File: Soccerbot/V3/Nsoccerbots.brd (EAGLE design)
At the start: 149.8 x 101.3 mm, 69 parts, among them CN2 1X4-CLEANBIG, IC1 LM340S-05, IC2 TB6612FNG, IC4 TB6612FNG, J3 1X5, J4 1X5, Q1 AOD417, SW2 SPST_TACT-EVQQ2, U1 PCA9685, X1 NXT-SOCKET, X2 NXT-SOCKET, X3 NXT-SOCKET, X4 NXT-SOCKET

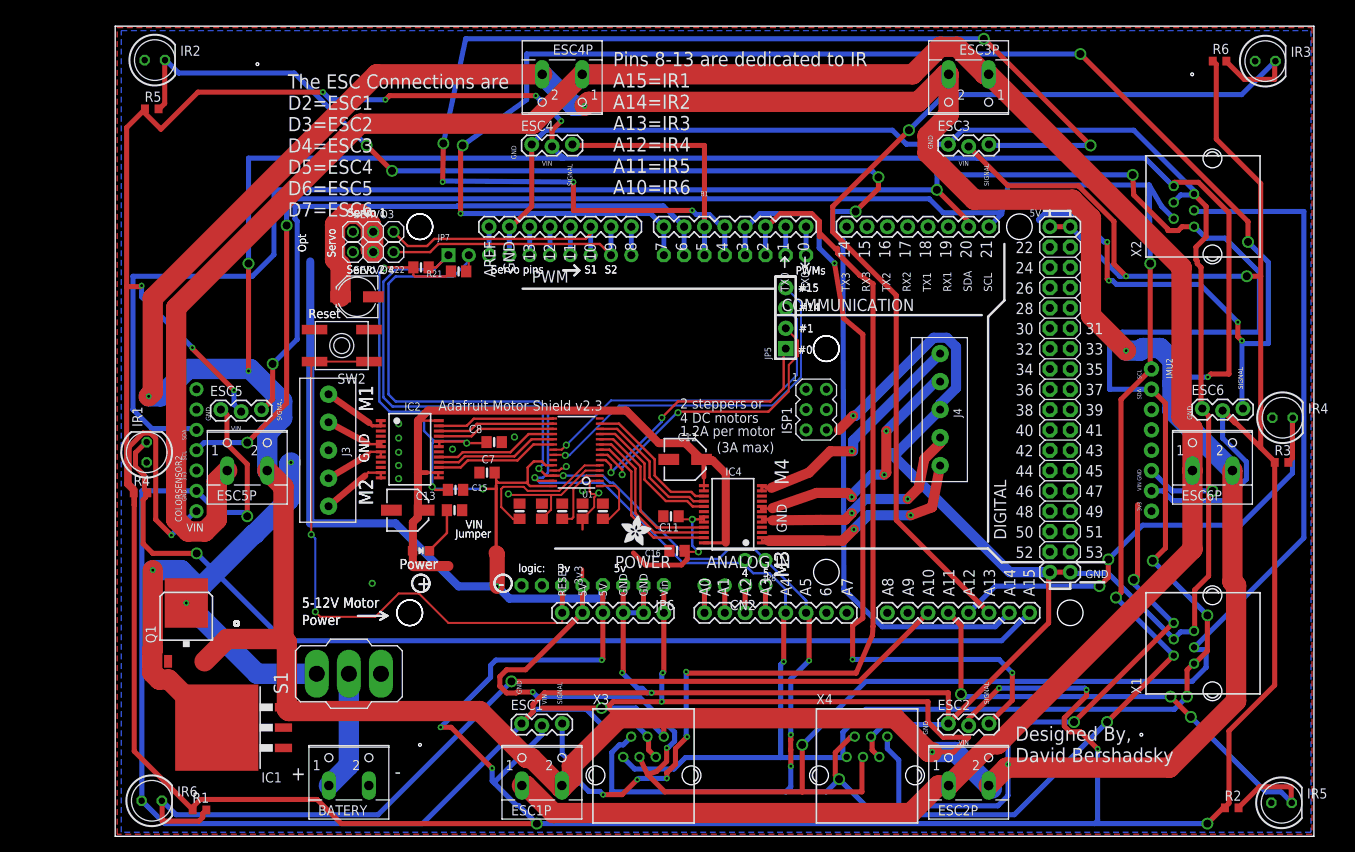
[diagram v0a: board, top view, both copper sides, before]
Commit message: Fully routed and all parts in
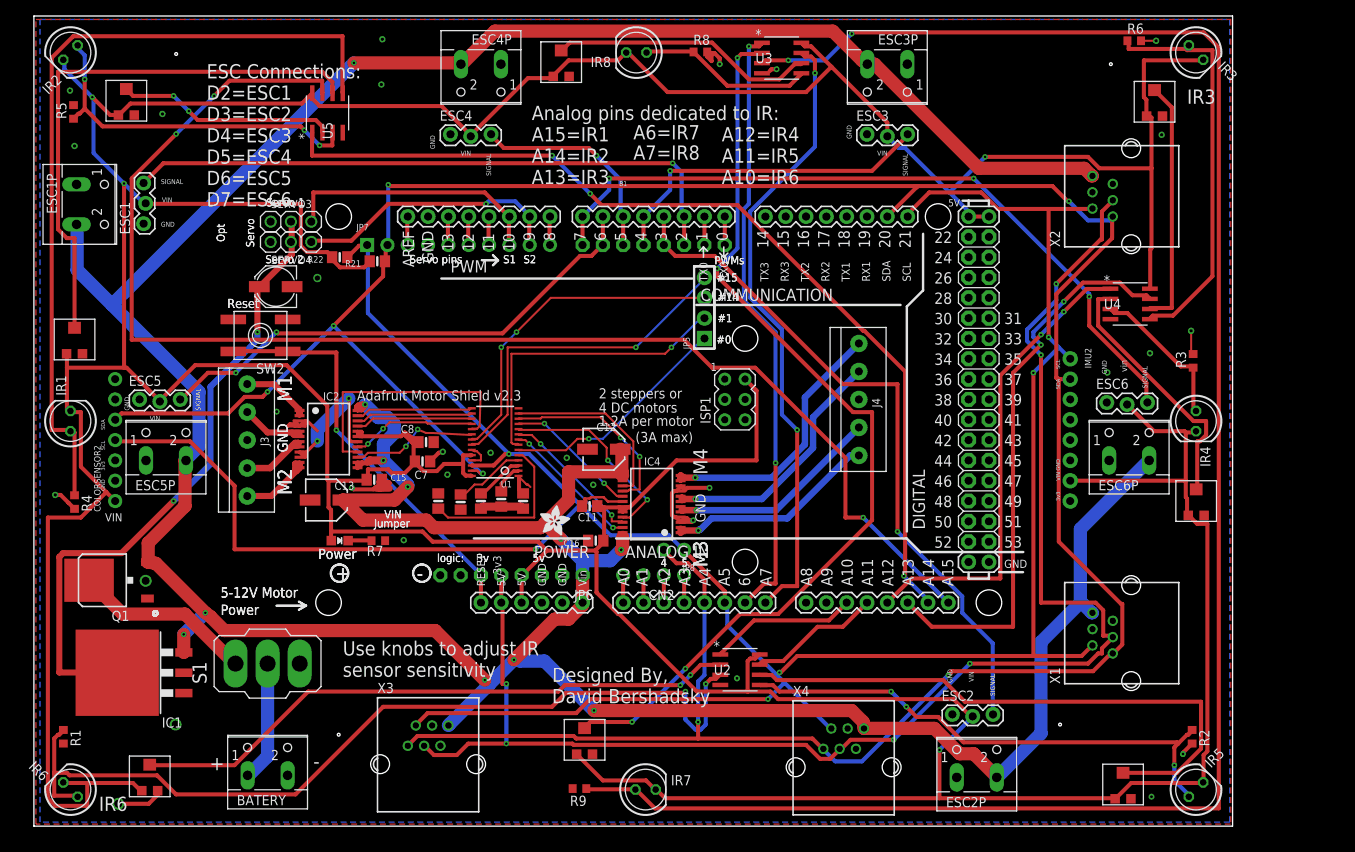
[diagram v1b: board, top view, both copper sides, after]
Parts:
- removed R18: 1K, microbuilder:0805-NO
- added IR7, IR8: (no value), led:LED5MM
- added IRP1, IRP2, IRP3, IRP4, IRP5, IRP6, IRP7, IRP8: TRIMPOT, trimPot:TRIMPOT
- added R7: 300ohm, rcl:R0603
- added R8, R9: 10k, adafruit:R0603
- added U2, U3, U4, U5: LM358DT, LM358DT:D8
- R1, R2, R3, R4, R5, R6: value (none) -> 10k
- moved ESC1P 91.3 mm to (6.60, 77.7), turned to 270 degrees
- moved ESC1 78.4 mm to (13.8, 75.3), turned to 90 degrees
- moved X3 27.0 mm to (49.3, 7.75)
- moved R1 19.3 mm to (3.68, 11.2), turned to 270 degrees
- moved R3 16.8 mm to (144.9, 58.2), turned to 90 degrees
- moved IC1 14.2 mm to (13.0, 19.2)
- moved ESC6 12.0 mm to (134.1, 52.8)
- moved Q1 11.0 mm to (9.40, 30.7), turned to 90 degrees
- moved R6 11.0 mm to (137.5, 98.2)
- moved IR4 10.8 mm to (145.3, 50.6), turned to 270 degrees
- moved IR5 10.8 mm to (145.3, 4.57), turned to 45 degrees
- moved IR2 10.6 mm to (4.57, 96.7), turned to 225 degrees
- moved ESC6P 10.5 mm to (136.9, 47.0)
- moved SERVO3 10.4 mm to (32.1, 75.6)
- moved SERVO4 10.4 mm to (32.1, 73.0)
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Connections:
- removed net GND1: IR5.A
- removed net GND2: IR4.A
- removed net GND3: IR1.A
- removed net GND4: IR2.A
- removed net GND5: IR3.A
- removed net VCC: ISP1.2
- new net IR1O+: IR1.A, R4.1, U5.5
- new net IR2O+: IR2.A, R5.1, U5.3
- new net IR3O+: IR3.A, R6.1, U4.5
- new net IR4O+: IR4.A, R3.1, U4.3
- new net IR5O+: IR5.A, R2.1, U2.5
- new net IR6O+: IR6.A, R1.1, U2.3
- new net IR7O+: IR7.A, R9.1, U3.3
- new net IR8O+: IR8.A, R8.1, U3.5
- new net N$11: IRP6.OUT, U2.2
- new net N$14: IRP5.OUT, U2.6
- new net N$17: IRP8.OUT, U3.6
- new net N$18: IRP3.OUT, U4.6
- new net N$21: IRP4.OUT, U4.2
- new net N$24: IRP2.OUT, U5.2
- new net N$27: IRP1.OUT, U5.6
- new net N$6: IRP7.OUT, U3.2
- net 5.5V: now also IR1.K, IR2.K, IR3.K, IR4.K, IR5.K, IR6.K, IR7.K, IR8.K, IRP1.VCC, IRP2.VCC, IRP3.VCC, IRP4.VCC, IRP5.VCC, IRP6.VCC, IRP7.VCC, IRP8.VCC, ISP1.2, LED2.A, U2.8, U3.8, U4.8, U5.8; no longer R1.1, R2.1, R3.1, R4.1, R5.1, R6.1
- net A10: now also U2.1; no longer IR6.K, R1.2
- net A11: now also U2.7; no longer IR5.K, R2.2
- net A12: now also U4.1; no longer IR4.K, R3.2
- net A13: now also U4.7; no longer IR3.K, R6.2
- net A14: now also U5.1; no longer IR2.K, R5.2
- net A15: now also U5.7; no longer IR1.K, R4.2
- net A6: now also U3.1
- net A7: now also U3.7
- net BAT+: no longer LED2.A
- net GND: now also IRP1.GND, IRP2.GND, IRP3.GND, IRP4.GND, IRP5.GND, IRP6.GND, IRP7.GND, IRP8.GND, R1.2, R2.2, R3.2, R4.2, R5.2, R6.2, R7.1, R8.2, R9.2, U2.4, U3.4, U4.4, U5.4; no longer IR6.A, R18.1
- net N$1: now also R7.2; no longer R18.2
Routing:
- net GND: track 846.5 -> 87.7 mm, vias 15 -> 32
- net BAT+: track 878.3 -> 486.8 mm, vias 13 -> 11
- net IR7O+: track 0.00 -> 234.7 mm, vias 0 -> 2
- net D7: track 217.2 -> 92.3 mm, vias 8 -> 3
- net N$6: track 0.00 -> 118.3 mm, vias 0 -> 4
- net D4: track 157.9 -> 42.3 mm, vias 6 -> 1
- net IR6O+: track 0.00 -> 111.3 mm, vias 0 -> 2
- net SDA: track 473.0 -> 364.5 mm
- net IR1O+: track 0.00 -> 102.0 mm
- net SCL: track 442.7 -> 344.0 mm, vias 11 -> 6
- net A10: track 115.9 -> 18.5 mm, vias 1 -> 0
- net A7: track 0.00 -> 78.4 mm, vias 0 -> 2
- net N$11: track 0.00 -> 76.5 mm, vias 0 -> 2
- net A6: track 0.00 -> 75.7 mm, vias 0 -> 2
- net N$14: track 0.00 -> 73.4 mm
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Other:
- board text added: "A12=IR4 A11=IR5 A10=IR6"
- board text added: "A6=IR7"
- board text added: "A7=IR8"
- board text added: "Analog pins dedicated to IR: A15=IR1 A14=IR2 A13=IR3"
- board text added: "ESC Connections: D2=ESC1 D3=ESC2 D4=ESC3 D5=ESC4 D6=ESC5 D7=ESC6"
- board text added: "IR3"
- board text added: "IR6"
- board text added: "Use knobs to adjust IR sensor sensitivity"
- board text added: "vin"
- board text removed: "Pins 8-13 are dedicated to IR A15=IR1 A14=IR2 A13=IR3 A12=IR4 A11=IR5 A10=IR6"
- board text removed: "The ESC Connections are D2=ESC1 D3=ESC2 D4=ESC3 D5=ESC4 D6=ESC5 D7=ESC6"

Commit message: added resistors
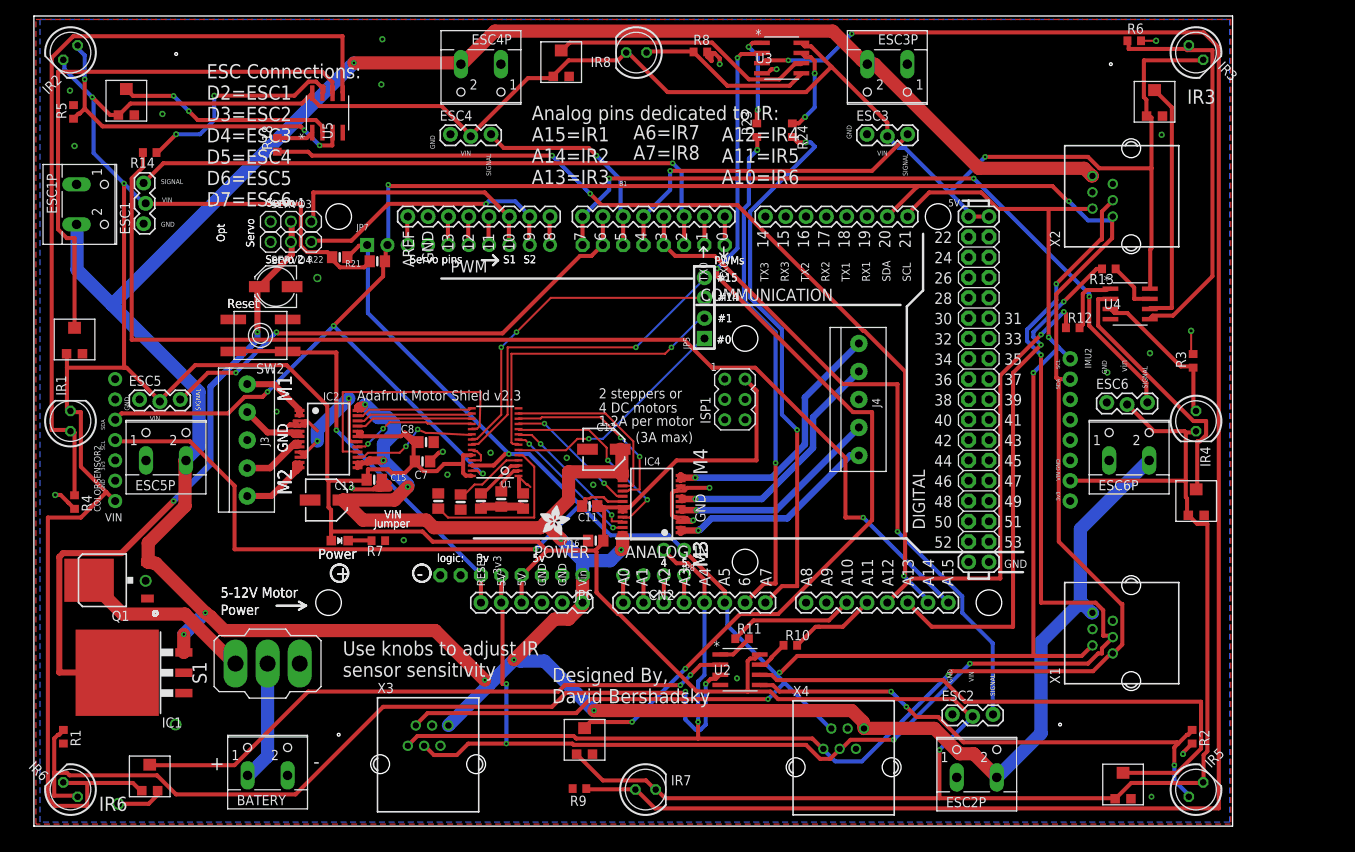
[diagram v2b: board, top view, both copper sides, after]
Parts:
- added R10, R11, R12, R13, R14, R18, R23, R24: 330ohms, resistor:R0603
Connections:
- new net N$10: R14.1, U5.7
- new net N$12: R18.2, U5.1
- new net N$13: R23.2, U3.1
- new net N$15: R24.1, U3.7
- new net N$2: R10.1, U2.7
- new net N$7: R11.2, U2.1
- new net N$8: R12.2, U4.1
- new net N$9: R13.1, U4.7
- net A10: now also R11.1; no longer U2.1
- net A11: now also R10.2; no longer U2.7
- net A12: now also R12.1; no longer U4.1
- net A13: now also R13.2; no longer U4.7
- net A14: now also R18.1; no longer U5.1
- net A15: now also R14.2; no longer U5.7
- net A6: now also R23.1; no longer U3.1
- net A7: now also R24.2; no longer U3.7
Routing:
- net N$10: track 0.00 -> 27.5 mm, vias 0 -> 2
- net A15: track 170.7 -> 144.0 mm, vias 3 -> 1
- net A6: track 75.7 -> 63.0 mm
- net N$13: track 0.00 -> 12.0 mm, vias 0 -> 2
- net N$15: track 0.00 -> 11.5 mm, vias 0 -> 2
- net A7: track 78.4 -> 68.9 mm
- net N$8: track 0.00 -> 8.09 mm
- net N$9: track 0.00 -> 6.67 mm
- net A13: track 71.1 -> 65.0 mm
- net A11: track 16.6 -> 11.2 mm
- net A12: track 59.0 -> 54.1 mm
- net N$12: track 0.00 -> 4.67 mm
- net N$7: track 0.00 -> 4.38 mm
- net N$2: track 0.00 -> 4.03 mm
- net A10: track 18.5 -> 15.8 mm
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
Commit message: x
x
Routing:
- net 5.5V: track 773.9 -> 777.9 mm
- net M1B1: track 8.64 -> 9.96 mm
- net BAT+: track 486.8 -> 488.1 mm
- net GND: track 87.7 -> 88.9 mm
- net M3B1: track 26.7 -> 27.7 mm
- net M4B1: track 31.4 -> 32.2 mm
- net M2B1: track 8.85 -> 9.63 mm
- net M2A1: track 10.6 -> 11.2 mm
- net M3A1: track 26.8 -> 27.4 mm
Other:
- board text removed: "(3A max)"
- board text removed: "1.2A per motor"
- board text removed: "2 steppers or"
- board text removed: "4 DC motors"
- board text removed: "Adafruit Motor Shield v2! Control 4 DC Motors or 2 Stepper motors via I2C Pins used: SDA, SCL & A4 tied to SDA, A5 to SCL"
- board text removed: "Adafruit Motor Shield v2.3"
- board text removed: "For opt. servo"
- board text removed: "pwr supply cut trace"

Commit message: Misc Changes
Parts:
- removed S1: (no value), switch:320-916
- added U$2: TOGGLESWITCH, toggleswitch:TOGGLESWITCH
- R7: value 300ohm -> 150ohm
- moved BATERY 0.85 mm to (29.4, 8.45)
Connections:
- net N$4: now also U$2.IN; no longer S1.2
- net N$5: now also U$2.OUT; no longer S1.1
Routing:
- net N$11: track 76.5 -> 87.3 mm
- net N$5: track 22.6 -> 25.5 mm
- net IR6O+: track 111.3 -> 111.9 mm
- net GND: vias 32 -> 33
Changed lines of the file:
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@@
 <?xml version="1.0" encoding="utf-8"?>
 <!DOCTYPE eagle SYSTEM "eagle.dtd">
-<eagle version="8.4.1">
+<eagle version="8.4.3">
 <drawing>
 <settings>
@@
 <attribute name="OC_NEWARK" value="unknown" x="129.54" y="49.53" size="1.778" layer="27" rot="R270" display="off"/>
 </element>
-<element name="S1" library="switch" package="320-916" value="" x="29.21" y="20.32" rot="R90">
-<attribute name="MF" value="" x="29.21" y="20.32" size="1.778" layer="27" rot="R90" display="off"/>
-<attribute name="MPN" value="" x="29.21" y="20.32" size="1.778" layer="27" rot="R90" display="off"/>
-<attribute name="OC_NEWARK" value="unknown" x="29.21" y="20.32" size="1.778" layer="27" rot="R90" display="off"/>
-</element>
 <element name="X1" library="NXT Compatible (female) Sockets - Mindsensors" package="NXT-SOCKET" value="NXT-SOCKET" x="137.16" y="24.13" rot="R90">
 <attribute name="MF" value="" x="137.16" y="24.13" size="1.778" layer="27" rot="R90" display="off"/>
@@
 <attribute name="OC_NEWARK" value="04R6830" x="55.88" y="93.98" size="1.778" layer="27" rot="R180" display="off"/>
 </element>
-<element name="BATERY" library="con-wago-500" library_urn="urn:adsk.eagle:library:195" package="W237-102" value="" x="29.21" y="7.62">
-<attribute name="MF" value="" x="29.21" y="7.62" size="1.778" layer="27" display="off"/>
-<attribute name="MPN" value="MA522-500M02" x="29.21" y="7.62" size="1.778" layer="27" display="off"/>
-<attribute name="OC_FARNELL" value="unknown" x="29.21" y="7.62" size="1.778" layer="27" display="off"/>
-<attribute name="OC_NEWARK" value="04R6830" x="29.21" y="7.62" size="1.778" layer="27" display="off"/>
+<element name="BATERY" library="con-wago-500" library_urn="urn:adsk.eagle:library:195" package="W237-102" value="" x="29.4005" y="8.4455">
+<attribute name="MF" value="" x="29.4005" y="8.4455" size="1.778" layer="27" display="off"/>
+<attribute name="MPN" value="MA522-500M02" x="29.4005" y="8.4455" size="1.778" layer="27" display="off"/>
+<attribute name="OC_FARNELL" value="unknown" x="29.4005" y="8.4455" size="1.778" layer="27" display="off"/>
+<attribute name="OC_NEWARK" value="04R6830" x="29.4005" y="8.4455" size="1.778" layer="27" display="off"/>
 </element>
 <element name="ISP1" library="adafruit" library_urn="urn:adsk.eagle:library:420" package="AVRISP" value="AVRISP-6" x="87.63" y="53.34">
@@
 <attribute name="OC_NEWARK" value="01AC5221" x="12.954" y="19.177" size="1.778" layer="27" rot="R90" display="off"/>
 </element>
-<element name="R7" library="rcl" library_urn="urn:adsk.eagle:library:334" package="R0603" package3d_urn="urn:adsk.eagle:package:23555/2" value="300ohm" x="43.053" y="35.687" rot="R180">
+<element name="R7" library="rcl" library_urn="urn:adsk.eagle:library:334" package="R0603" package3d_urn="urn:adsk.eagle:package:23555/2" value="150ohm" x="43.053" y="35.687" rot="R180">
 <attribute name="MF" value="" x="43.053" y="35.687" size="1.778" layer="27" rot="R180" display="off"/>
 <attribute name="MPN" value="" x="43.053" y="35.687" size="1.778" layer="27" rot="R180" display="off"/>
@@
 <attribute name="OC_NEWARK" value="68R2991" x="94.8055" y="86.995" size="1.778" layer="27" rot="R270" display="off"/>
 </element>
+<element name="U$2" library="toggleswitch" package="TOGGLESWITCH" value="TOGGLESWITCH" x="33.274" y="19.1135" rot="R270"/>
 </elements>
 <signals>
@@
 <wire x1="33.205" y1="46.112" x2="33.3795" y2="46.2865" width="0.1524" layer="1"/>
 <wire x1="33.3795" y1="46.2865" x2="33.3795" y2="46.5875" width="0.1524" layer="1"/>
+<via x="37.084" y="6.35" extent="1-16" drill="0.85"/>
 </signal>
 <signal name="D3">
@@
 </signal>
 <signal name="N$4" class="1">
-<contactref element="S1" pad="2"/>
 <contactref element="BATERY" pad="1"/>
-<wire x1="29.21" y1="8.73125" x2="26.82875" y2="6.35" width="1.651" layer="16"/>
-<wire x1="29.21" y1="20.32" x2="29.21" y2="8.73125" width="1.651" layer="16"/>
-<wire x1="26.82875" y1="6.35" x2="26.71" y2="6.35" width="1.651" layer="16"/>
+<contactref element="U$2" pad="IN"/>
+<wire x1="26.9005" y1="7.1755" x2="33.274" y2="13.549" width="1.651" layer="1"/>
+<wire x1="33.274" y1="13.549" x2="33.274" y2="19.1135" width="1.651" layer="1"/>
 </signal>
 <signal name="M1A1" class="2">
@@
 <contactref element="JP6" pad="8"/>
 </signal>
-<signal name="N$5" class="1">
-<contactref element="S1" pad="1"/>
-<contactref element="Q1" pad="4"/>
-<wire x1="18.89125" y1="26.51125" x2="25.0825" y2="20.32" width="1.651" layer="1"/>
-<wire x1="11.1125" y1="26.51125" x2="18.89125" y2="26.51125" width="1.651" layer="1"/>
-<wire x1="6.985" y1="30.63875" x2="11.1125" y2="26.51125" width="1.651" layer="1"/>
-<wire x1="25.0825" y1="20.32" x2="25.1968" y2="20.32" width="1.651" layer="1"/>
-<wire x1="6.985" y1="30.63875" x2="6.898" y2="30.734" width="1.651" layer="1"/>
-</signal>
 <signal name="SERVO5V" class="2">
 <contactref element="SERVO4" pad="2"/>
@@
 <wire x1="81.28" y1="16.66875" x2="81.43875" y2="16.8275" width="0.508" layer="1"/>
 <wire x1="66.51625" y1="16.66875" x2="81.28" y2="16.66875" width="0.508" layer="1"/>
-<wire x1="64.77" y1="14.9225" x2="66.51625" y2="16.66875" width="0.508" layer="1"/>
-<wire x1="43.65625" y1="14.9225" x2="64.77" y2="14.9225" width="0.508" layer="1"/>
-<wire x1="32.7025" y1="3.96875" x2="43.65625" y2="14.9225" width="0.508" layer="1"/>
-<wire x1="17.78" y1="3.96875" x2="32.7025" y2="3.96875" width="0.508" layer="1"/>
-<wire x1="15.39875" y1="6.35" x2="17.78" y2="3.96875" width="0.508" layer="1"/>
+<wire x1="66.51625" y1="16.66875" x2="64.77" y2="14.9225" width="0.508" layer="1"/>
+<wire x1="17.78" y1="3.96875" x2="15.39875" y2="6.35" width="0.508" layer="1"/>
 <wire x1="4.445" y1="6.35" x2="15.39875" y2="6.35" width="0.508" layer="1"/>
 <wire x1="4.1275" y1="6.6675" x2="4.445" y2="6.35" width="0.508" layer="1"/>
@@
 <via x="83.97875" y="17.78" extent="1-16" drill="0.3"/>
 <via x="81.43875" y="16.8275" extent="1-16" drill="0.3"/>
+<wire x1="28.25559375" y1="6.71298125" x2="28.25559375" y2="5.71885" width="0.508" layer="1"/>
+<wire x1="28.25559375" y1="5.71885" x2="27.4618" y2="4.92505625" width="0.508" layer="1"/>
+<wire x1="36.4651125" y1="14.9225" x2="28.25559375" y2="6.71298125" width="0.508" layer="1"/>
+<wire x1="18.73630625" y1="4.92505625" x2="17.78" y2="3.96875" width="0.508" layer="1"/>
+<wire x1="27.4618" y1="4.92505625" x2="18.73630625" y2="4.92505625" width="0.508" layer="1"/>
+<wire x1="64.77" y1="14.9225" x2="36.4651125" y2="14.9225" width="0.508" layer="1"/>
 </signal>
 <signal name="IR5O+">
@@
 <contactref element="U2" pad="2"/>
 <contactref element="IRP6" pad="OUT"/>
-<wire x1="25.0825" y1="7.62" x2="14.605" y2="7.62" width="0.508" layer="1"/>
-<wire x1="34.29" y1="16.8275" x2="25.0825" y2="7.62" width="0.508" layer="1"/>
-<wire x1="65.56375" y1="16.8275" x2="34.29" y2="16.8275" width="0.508" layer="1"/>
+<wire x1="65.56375" y1="16.8275" x2="38.481" y2="16.764" width="0.508" layer="1"/>
 <wire x1="66.3575" y1="17.62125" x2="65.56375" y2="16.8275" width="0.508" layer="1"/>
 <wire x1="80.80375" y1="17.62125" x2="66.3575" y2="17.62125" width="0.508" layer="1"/>
@@
 <wire x1="83.34375" y1="20.16125" x2="82.07375" y2="18.89125" width="0.508" layer="1"/>
 <wire x1="85.725" y1="20.16125" x2="83.34375" y2="20.16125" width="0.508" layer="1"/>
-<wire x1="14.605" y1="7.62" x2="14.478" y2="7.6835" width="0.508" layer="1"/>
+<wire x1="14.478" y1="7.6835" x2="14.605" y2="7.62" width="0.508" layer="1"/>
 <wire x1="85.725" y1="20.16125" x2="85.8012" y2="20.193" width="0.508" layer="1"/>
 <via x="80.80375" y="17.62125" extent="1-16" drill="0.3"/>
 <via x="82.07375" y="18.89125" extent="1-16" drill="0.3"/>
+<wire x1="36.7182375" y1="22.288425" x2="36.448925" y2="22.5577375" width="0.508" layer="1"/>
+<wire x1="36.448925" y1="22.5577375" x2="30.099075" y2="22.5577375" width="0.508" layer="1"/>
+<wire x1="29.7078375" y1="15.938575" x2="29.438525" y2="15.6692625" width="0.508" layer="1"/>
+<wire x1="38.481" y1="16.764" x2="36.7182375" y2="18.5267625" width="0.508" layer="1"/>
+<wire x1="36.7182375" y1="18.5267625" x2="36.7182375" y2="22.288425" width="0.508" layer="1"/>
+<wire x1="22.4637625" y1="15.6692625" x2="14.478" y2="7.6835" width="0.508" layer="1"/>
+<wire x1="29.438525" y1="15.6692625" x2="22.4637625" y2="15.6692625" width="0.508" layer="1"/>
+<wire x1="30.099075" y1="22.5577375" x2="29.7078375" y2="22.1665" width="0.508" layer="1"/>
+<wire x1="29.7078375" y1="22.1665" x2="29.7078375" y2="15.938575" width="0.508" layer="1"/>
 </signal>
 <signal name="N$14">
@@
 <wire x1="97.5995" y1="89.8525" x2="97.5995" y2="94.107" width="0.508" layer="16"/>
 </signal>
+<signal name="N$5" class="1">
+<contactref element="Q1" pad="4"/>
+<contactref element="U$2" pad="OUT"/>
+<wire x1="26.2636" y1="19.1135" x2="19.818359375" y2="25.558740625" width="1.651" layer="1"/>
+<wire x1="19.818359375" y1="25.558740625" x2="19.701934375" y2="25.646059375" width="1.651" layer="1"/>
+<wire x1="19.701934375" y1="25.646059375" x2="18.80499375" y2="26.543" width="1.651" layer="1"/>
+<wire x1="18.80499375" y1="26.543" x2="8.763" y2="26.543" width="1.651" layer="1"/>
+<wire x1="8.763" y1="26.543" x2="6.898" y2="28.408" width="1.651" layer="1"/>
+<wire x1="6.898" y1="28.408" x2="6.898" y2="30.734" width="1.651" layer="1"/>
+</signal>
 </signals>
